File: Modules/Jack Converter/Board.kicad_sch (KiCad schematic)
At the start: 0 parts

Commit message: Started Jack Converter diagram
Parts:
- added J1, J2, J3, J4: AudioJack2_SwitchT, symbol Connector_Audio:AudioJack2_SwitchT
- added SW1, SW2: SW_SPDT_321, symbol Switch:SW_SPDT_321
- added TP1: TestPoint, symbol Connector:TestPoint
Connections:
- new net: J1.T, J2.T, TP1.1
- new net GND: J1.S, J2.S, J3.S, J4.S

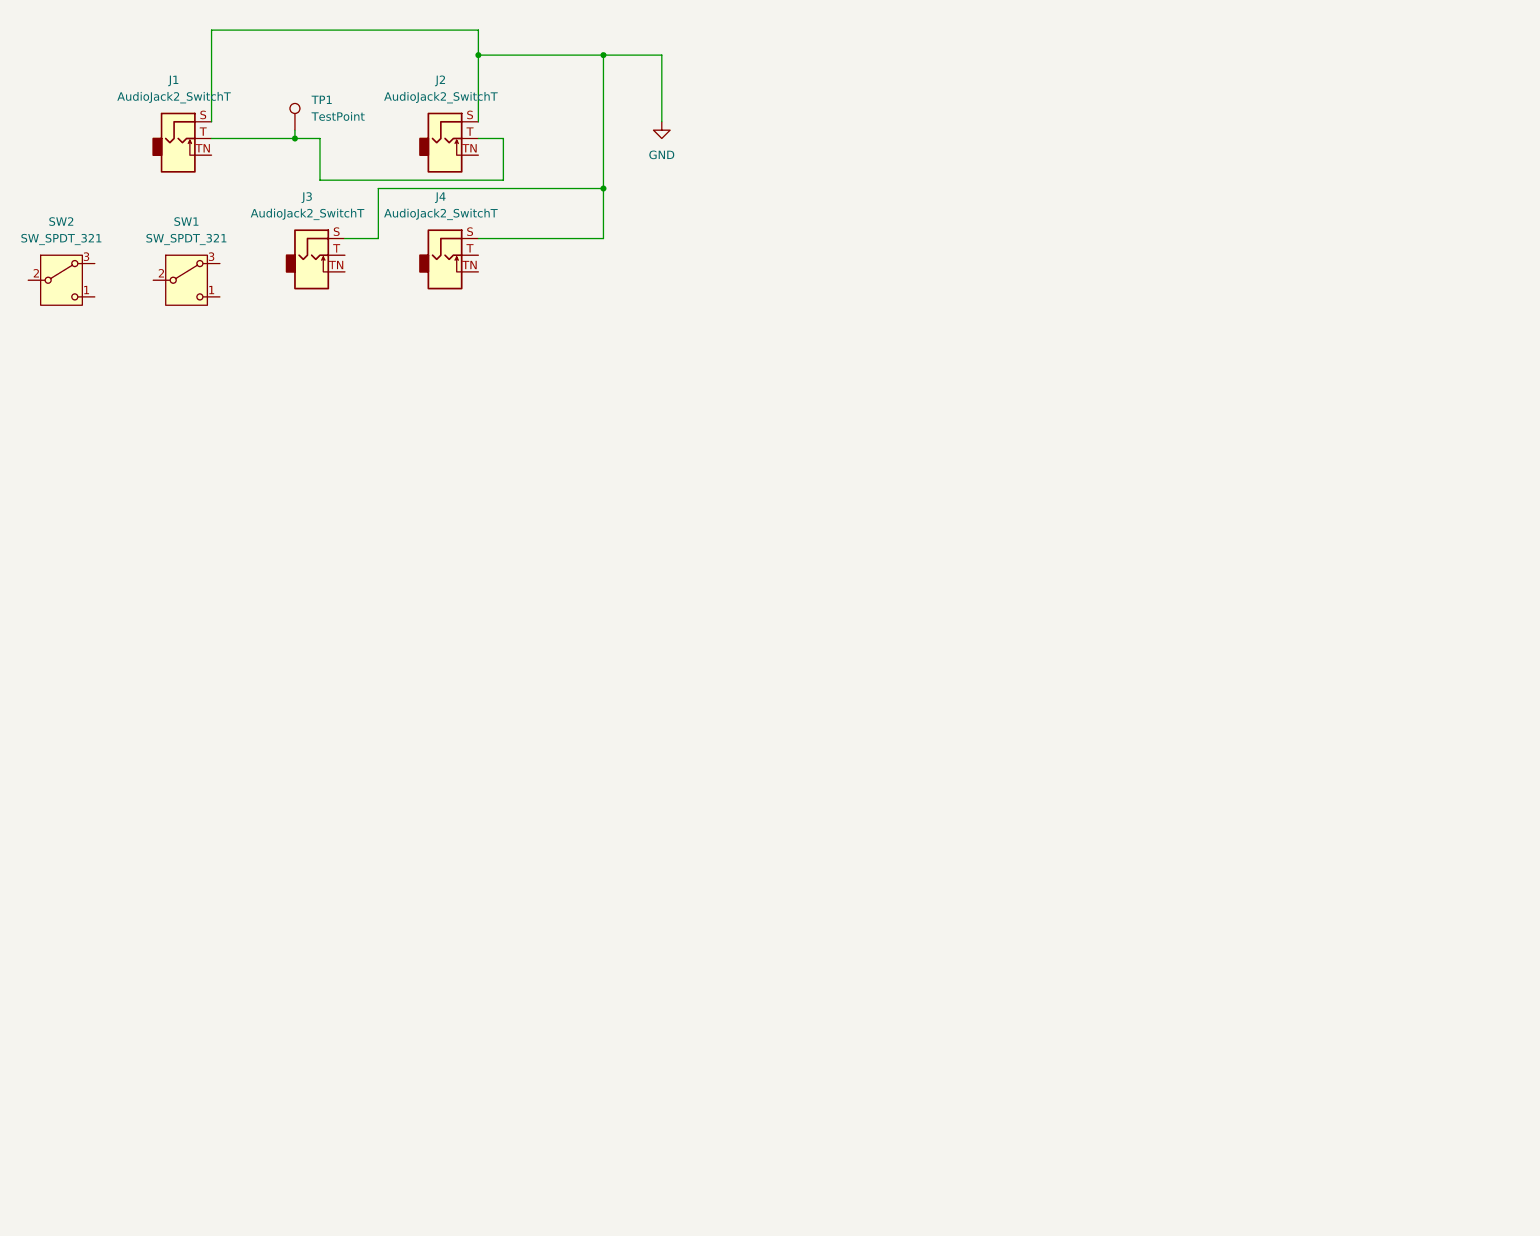
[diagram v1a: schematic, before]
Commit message: Nearly finished Jack Converter Mk1 schematic
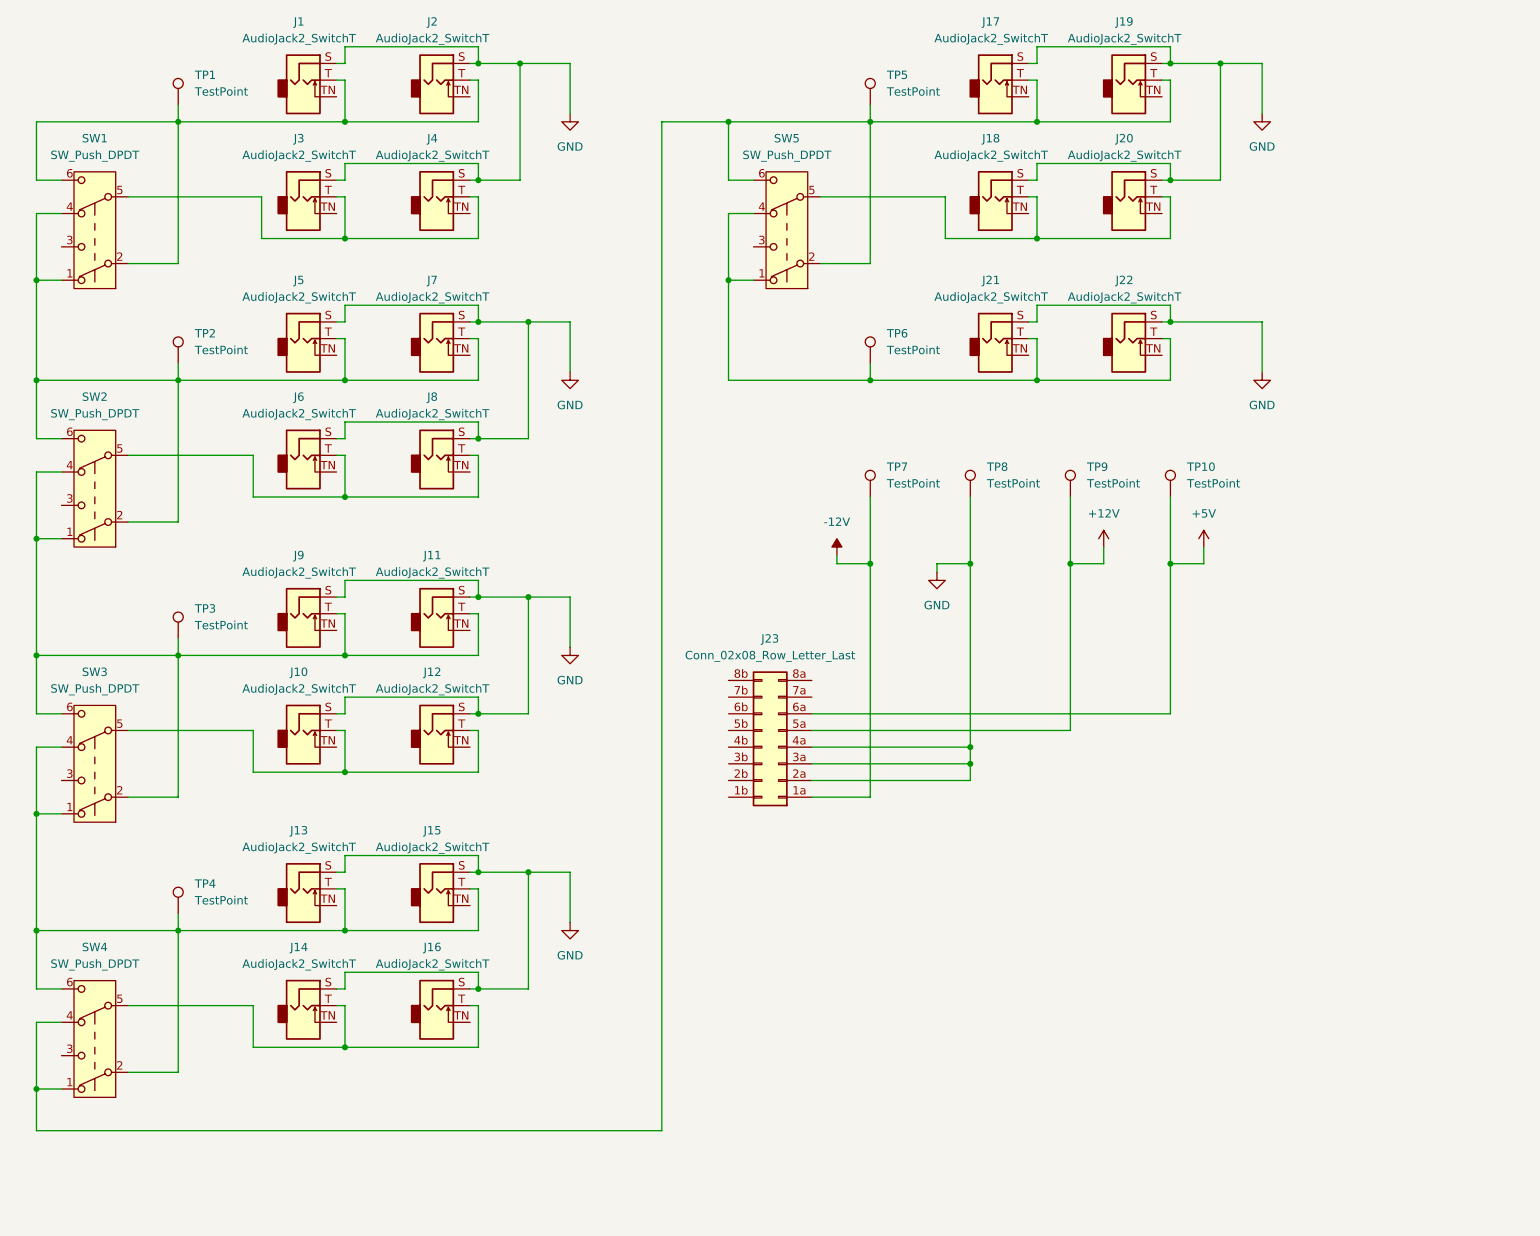
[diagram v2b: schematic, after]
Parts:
- removed SW1, SW2: SW_SPDT_321, symbol Switch:SW_SPDT_321
- added J10, J11, J12, J13, J14, J15, J16, J17, J18, J19, J20, J21, J22, J5, J6, J7, J8, J9: AudioJack2_SwitchT, symbol Connector_Audio:AudioJack2_SwitchT
- added J23: Conn_02x08_Row_Letter_Last, symbol Connector_Generic:Conn_02x08_Row_Letter_Last
- added SW1, SW2, SW3, SW4, SW5: SW_Push_DPDT, symbol Switch:SW_Push_DPDT
- added TP10, TP2, TP3, TP4, TP5, TP6, TP7, TP8, TP9: TestPoint, symbol Connector:TestPoint
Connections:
- net GND: now also J10.S, J11.S, J12.S, J13.S, J14.S, J15.S, J16.S, J17.S, J18.S, J19.S, J20.S, J21.S, J22.S, J23.2a (Pin_2a), J23.3a (Pin_3a), J23.4a (Pin_4a), J5.S, J6.S, J7.S, J8.S, J9.S, TP8.1
- net at J3.T: now also J4.T, SW1.5 (B)
- net at J1.T, J2.T, TP1.1: now also SW1.2 (B), SW1.6 (C)
- new net: J17.T, J19.T, SW4.1 (A), SW4.4 (A), SW5.2 (B), SW5.6 (C), TP5.1
- new net: J18.T, J20.T, SW5.5 (B)
- new net: J13.T, J15.T, SW3.1 (A), SW3.4 (A), SW4.2 (B), SW4.6 (C), TP4.1
- new net: J11.T, J9.T, SW2.1 (A), SW2.4 (A), SW3.2 (B), SW3.6 (C), TP3.1
- new net: J14.T, J16.T, SW4.5 (B)
- new net: J21.T, J22.T, SW5.1 (A), SW5.4 (A), TP6.1
- new net: J6.T, J8.T, SW2.5 (B)
- new net: J5.T, J7.T, SW1.1 (A), SW1.4 (A), SW2.2 (B), SW2.6 (C), TP2.1
- new net: J10.T, J12.T, SW3.5 (B)
- new net +12V: J23.5a (Pin_5a), TP9.1
- new net +5V: J23.6a (Pin_6a), TP10.1
- new net -12V: J23.1a (Pin_1a), TP7.1
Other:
- moved on the sheet: J1, J2, J3, J4, TP1

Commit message: Updated Jack Converter Mk1 symbol names and IDs
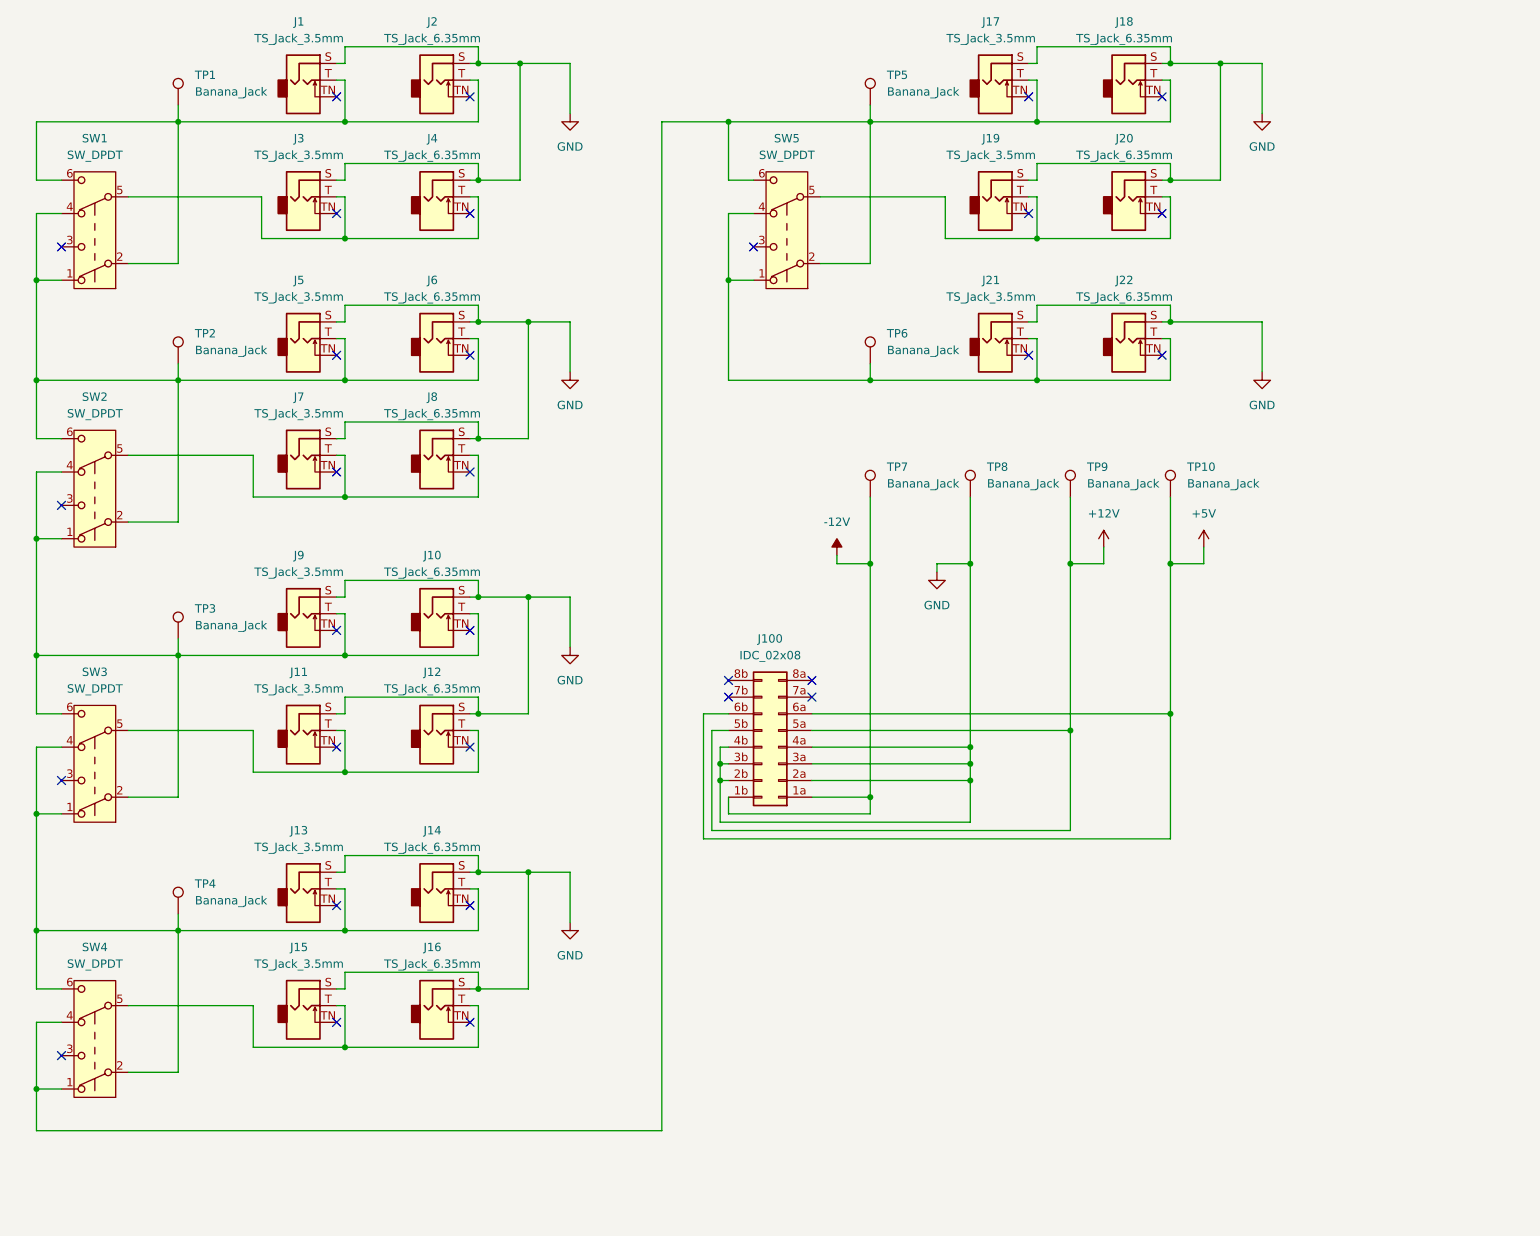
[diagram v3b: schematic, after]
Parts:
- J1, J13, J17, J21, J3, J5, J9: value AudioJack2_SwitchT -> TS_Jack_3.5mm
- J10: renamed from J11; value AudioJack2_SwitchT -> TS_Jack_6.35mm
- J100: renamed from J23; value Conn_02x08_Row_Letter_Last -> IDC_02x08
- J11: renamed from J10; value AudioJack2_SwitchT -> TS_Jack_3.5mm
- J12, J16, J2, J20, J22, J4, J8: value AudioJack2_SwitchT -> TS_Jack_6.35mm
- J14: renamed from J15; value AudioJack2_SwitchT -> TS_Jack_6.35mm
- J15: renamed from J14; value AudioJack2_SwitchT -> TS_Jack_3.5mm
- J18: renamed from J19; value AudioJack2_SwitchT -> TS_Jack_6.35mm
- J19: renamed from J18; value AudioJack2_SwitchT -> TS_Jack_3.5mm
- J6: renamed from J7; value AudioJack2_SwitchT -> TS_Jack_6.35mm
- J7: renamed from J6; value AudioJack2_SwitchT -> TS_Jack_3.5mm
- SW1, SW2, SW3, SW4, SW5: value SW_Push_DPDT -> SW_DPDT
- TP1, TP10, TP2, TP3, TP4, TP5, TP6, TP7, TP8, TP9: value TestPoint -> Banana_Jack
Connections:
- net +12V: now also J100.5b (Pin_5b)
- net +5V: now also J100.6b (Pin_6b)
- net -12V: now also J100.1b (Pin_1b)
- net GND: now also J100.2b (Pin_2b), J100.3b (Pin_3b), J100.4b (Pin_4b)
- no-connect marks 0 -> 31

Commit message: Converted 2 last jack rows to hardwired connections to backbone CV and Gate
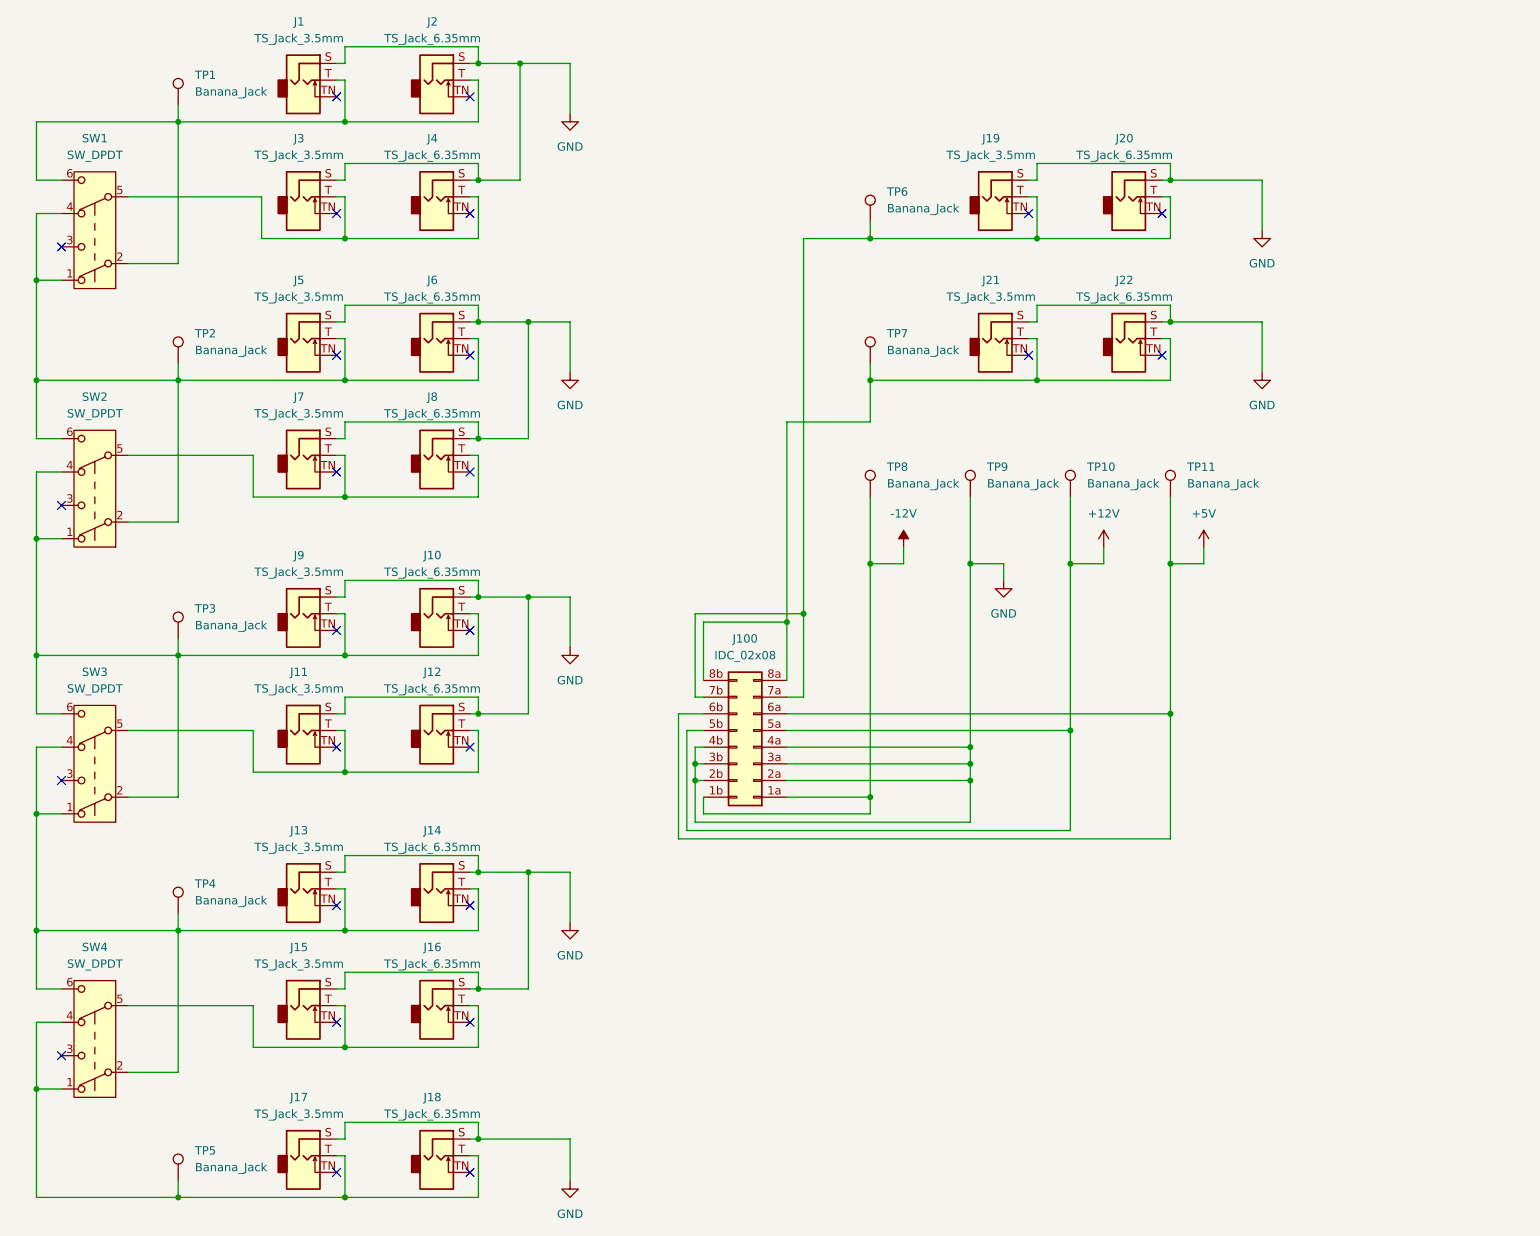
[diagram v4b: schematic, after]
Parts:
- removed SW5: SW_DPDT, symbol Switch:SW_Push_DPDT
- added TP6: Banana_Jack, symbol Connector:TestPoint
- renumbered TP9 to TP10, TP10 to TP11, TP6 to TP7, TP7 to TP8, TP8 to TP9
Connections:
- net at J19.T, J20.T: now also J100.7a (Pin_7a), J100.7b (Pin_7b), TP6.1
- net at J100.8a (Pin_8a): now also J100.8b (Pin_8b), J21.T, J22.T, TP7.1
- no-connect marks 31 -> 26
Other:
- moved on the sheet: J100, J17, J18, TP5
